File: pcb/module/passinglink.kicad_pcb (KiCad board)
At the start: 2 copper layers, 113.5 x 35 mm, 47 parts, among them J1 Conn_01x05_Female, J10 Conn_02x04_Odd_Even, J11 Conn_01x01, J12 Conn_01x04, J2 Conn_01x04, J3 Conn_02x05_Odd_Even, J4 Conn_01x05, J5 Conn_01x05, J6 Conn_02x08_Odd_Even, J7 Conn_02x08_Odd_Even, J8 Conn_01x03, J9 Conn_01x03, U1 STM32F103RETx, U2 MIC5219-3.3YM5, X1 PCB-USB-C, Y1 Crystal_GND2_Small

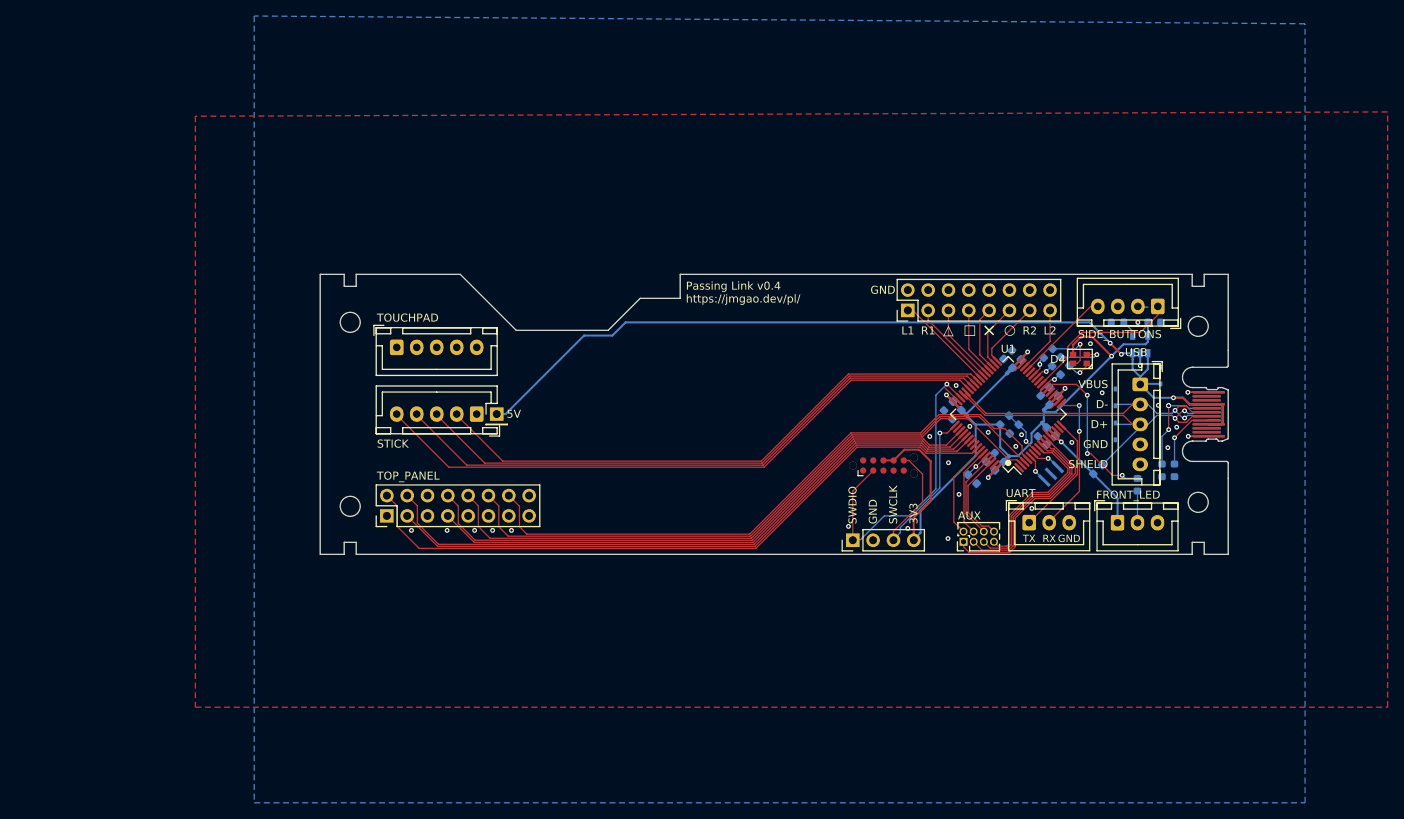
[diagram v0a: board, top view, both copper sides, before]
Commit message: PCB v0.5.
Layout a new PCB that connects to an external breakout board via an M.2
connector.
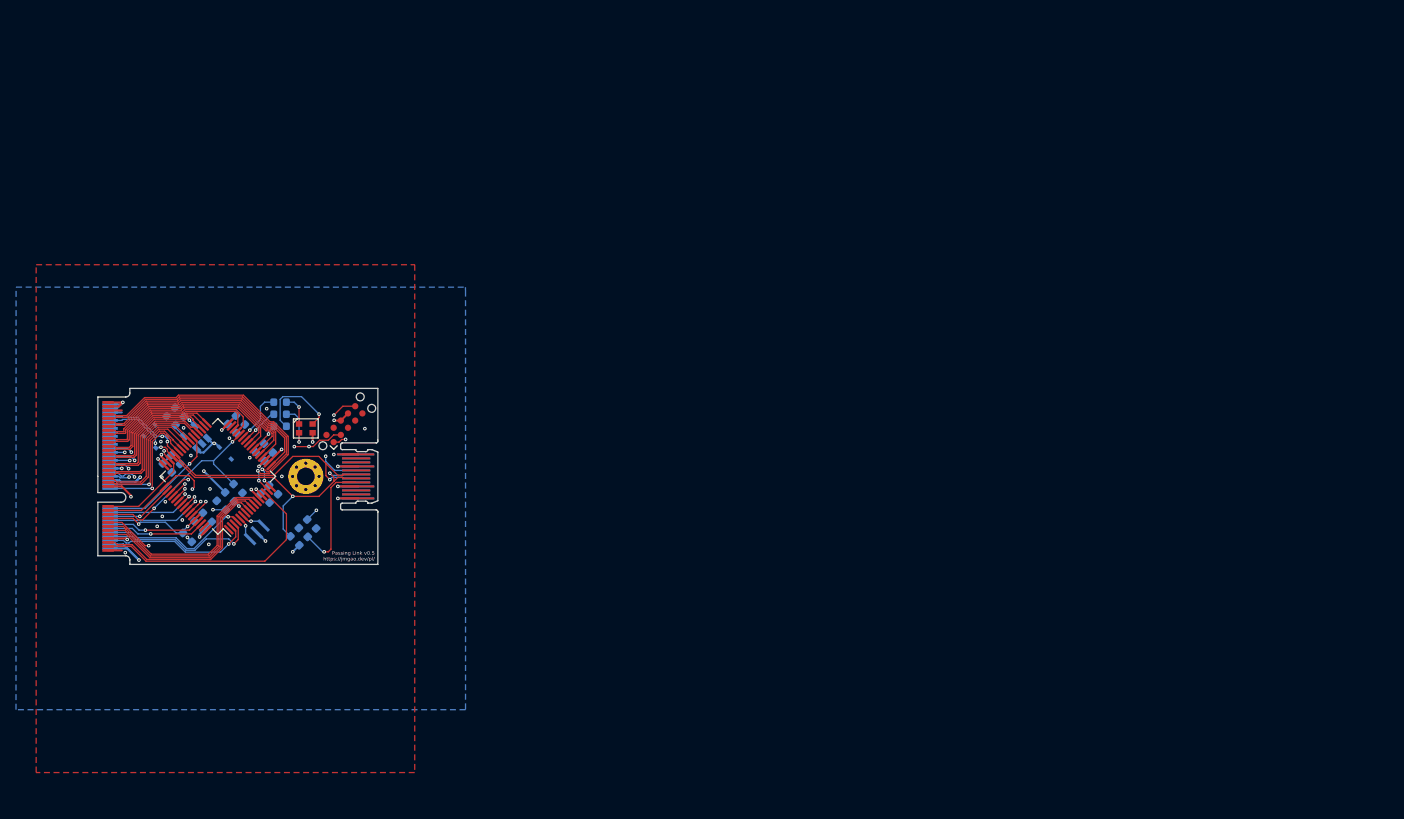
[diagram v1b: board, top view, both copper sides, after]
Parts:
- removed J1: Conn_01x05_Female, Connector_JST:JST_XH_B5B-XH-A_1x05_P2.50mm_Vertical
- removed J10: Conn_02x04_Odd_Even, Connector_PinHeader_1.27mm:PinHeader_2x04_P1.27mm_Vertical
- removed J11: Conn_01x01, Connector_PinHeader_2.54mm:PinHeader_1x01_P2.54mm_Vertical
- removed J12: Conn_01x04, Connector_JST:JST_XH_B4B-XH-A_1x04_P2.50mm_Vertical
- removed J4, J5: Conn_01x05, Connector_JST:JST_XH_B5B-XH-A_1x05_P2.50mm_Vertical
- removed J6, J7: Conn_02x08_Odd_Even, Connector_PinHeader_2.54mm:PinHeader_2x08_P2.54mm_Vertical
- removed J8, J9: Conn_01x03, Connector_JST:JST_XH_B3B-XH-A_1x03_P2.50mm_Vertical
- removed NT1, NT2, NT3, NT4, NT5: Net-Tie_2, NetTie:NetTie-2_SMD_Pad0.5mm
- removed the R4 at (219.6, 99.2)
- removed the R9 at (215.0, 101.0)
- added H1: MountingHole_2.2mm_M2_Pad_Via, MountingHole:MountingHole_2.2mm_M2_Pad_Via, F.Cu at (111.0, 100.0)
- added R1: 10K, Resistor_SMD:R_0603_1608Metric, B.Cu at (102.5, 101.5)
- added R5: 5.1K, Resistor_SMD:R_0603_1608Metric, B.Cu at (110.7, 107.0)
- J2: value Conn_01x04 -> PassingLink; footprint Connector_PinHeader_2.54mm:PinHeader_1x04_P2.54mm_Vertical -> NGFF:NGFF_E
- moved C1 122.4 mm to (95.2, 92.0), turned to 135 degrees
- moved D3 120.7 mm to (91.5, 95.7), turned to 135 degrees
- moved D2 119.4 mm to (92.9, 94.3), turned to 135 degrees
- moved C13 118.9 mm to (94.2, 93.0), turned to 135 degrees
- moved U2 118.6 mm to (97.2, 95.1), turned to 135 degrees
- moved D1 117.3 mm to (100.9, 97.1), turned to -45 degrees
- moved X1 106.6 mm to (120.0, 100.0)
- moved R4 106.5 mm to (111.7, 106.0), turned to -45 degrees
- moved R6 100.8 mm to (109.6, 108.0), turned to -45 degrees
- moved C12 99.6 mm to (100.4, 103.6), turned to 135 degrees
- moved Y1 99.5 mm to (104.9, 107.0)
- moved C7 99.5 mm to (105.3, 97.5)
- moved C5 99.2 mm to (98.7, 105.1)
- moved C10 99.2 mm to (97.6, 106.2)
- moved U1 99.1 mm to (100.0, 100.0)
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- renumbered R1 to R2, R2 to R3, R3 to R4, R5 to R6, R6 to R7, R7 to R8, R8 to R9
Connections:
- C1 pad 1: +3V3 -> VCC1
- C10 pad 1: VCC4 -> VCC1
- C11 pad 1: VDDA -> VCC1
- C3 pad 1: VCC2 -> VCC1
- C4 pad 1: VCC3 -> VCC1
- C5 pad 1: VCC4 -> VCC1
- C6 pad 1: VDDA -> VCC1
- C8 pad 1: VCC2 -> VCC1
- C9 pad 1: VCC3 -> VCC1
- D4 pad 3: +3V3 -> VCC1
- J2 pad 1: SWDIO -> GND
- J2 pad 2: GND -> VCC1
- J2 pad 3: SWCLK -> /PA0_ADC
- J2 pad 4: +3V3 -> VCC1
- J3 pad : GND -> (no net)
- J3 pad 1: Net-(J3-Pad1) -> /NRST
- J3 pad 2: SWDIO -> /PA13_SWDIO
- J3 pad 6: SWCLK -> /PA14_SWCLK
- J3 pad 7: +3V3 -> VCC1
- J3 pad 8: +3V3 -> VCC1
- R2 pad 2: +3V3 -> VCC1
- R6 pad 2: VDDA -> VCC1
- R7 pad 1: /PA7_LED_R_K -> /PB1_LED_R_K
- R9 pad 1: /PB1_LED_B_K -> /PA7_LED_B_K
- U1 pad 10: /PC2 -> /PC2_ADC
- U1 pad 11: /PC3 -> /PC3_ADC
- U1 pad 13: VDDA -> VCC1
- U1 pad 14: /PA0 -> /PA0_ADC
- U1 pad 15: /PA1 -> /PA1_ADC
- U1 pad 16: /PA2_UART_TX -> /PA2_ADC
- U1 pad 17: /PA3_UART_RX -> /PA3_ADC
- U1 pad 2: /PC13_MODE_LS -> /PC13
- U1 pad 20: /PA4 -> /PA4_DAC
- U1 pad 21: /PA5 -> /PA5_DAC
- U1 pad 22: /PA6_FRONT_LED_K -> /PA6_PWM
- U1 pad 23: /PA7_LED_R_K -> /PA7_LED_B_K
- U1 pad 24: /PC4_START -> /PC4_ADC
- U1 pad 25: /PC5 -> /PC5_ADC
- U1 pad 27: /PB1_LED_B_K -> /PB1_LED_R_K
- U1 pad 28: /PB2 -> /BOOT1
- U1 pad 29: /PB10_SELECT -> /PB10_I2C2_SCL
- U1 pad 3: /PC14_MODE_LOCK -> /PC14
- U1 pad 30: /PB11_BUTTON_L2 -> /PB11_I2C2_SDA
- U1 pad 32: VCC2 -> VCC1
- U1 pad 33: /PB12_BUTTON_R2 -> /PB12_SPI1_NSS
- U1 pad 34: /PB13_BUTTON_CIRCLE -> /PB13_SPI1_SCK
- U1 pad 35: /PB14_BUTTON_CROSS -> /PB14_SPI1_MISO
- U1 pad 36: /PB15_BUTTON_SQUARE -> /PB15_SPI1_MOSI
- U1 pad 37: /PC6_BUTTON_TRIANGLE -> /PC6
- U1 pad 38: /PC7_BUTTON_R1 -> /PC7_I2S3_MCK
- U1 pad 39: /PC8_BUTTON_L1 -> /PC8
- U1 pad 4: /PC15_BUTTON_PS4 -> /PC15
- U1 pad 40: /PC9_STICK_RIGHT -> /PC9
- U1 pad 41: /PA8_STICK_LEFT -> /PA8
- U1 pad 42: /PA9_STICK_UP -> /PA9_UART_TX
- U1 pad 43: /PA10_STICK_DOWN -> /PA10_UART_RX
- U1 pad 46: SWDIO -> /PA13_SWDIO
- U1 pad 48: VCC3 -> VCC1
- U1 pad 49: SWCLK -> /PA14_SWCLK
- U1 pad 50: /PA15_JTDI -> /PA15_I2S3_WS
- U1 pad 51: /PC10_MODE_RS -> /PC10
- U1 pad 52: /PC11_MODE_PS3 -> /PC11
- U1 pad 53: /PC12_BUTTON_L3 -> /PC12
- U1 pad 54: /PD2_BUTTON_R3 -> /PD2
- U1 pad 55: /PB3_JTDO -> /PB3_I2S3_CK
- U1 pad 57: /PB5_BUTTON_TOUCHPAD -> /PB5_I2S3_SD
- U1 pad 58: /PB6 -> /PB6_I2C1_SCL
- U1 pad 59: /PB7 -> /PB7_I2C1_SDA
- U1 pad 61: /PB8 -> /PB8_PWM
- U1 pad 62: /PB9 -> /PB9_PWM
- U1 pad 64: VCC4 -> VCC1
- U1 pad 8: /PC0 -> /PC0_ADC
- U1 pad 9: /PC1 -> /PC1_ADC
- U2 pad 5: +3V3 -> VCC1
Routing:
- net +3V3: track 86.6 -> 0.00 mm, vias 1 -> 0
- net /PB5_BUTTON_TOUCHPAD: track 83.9 -> 0.00 mm
- net /PC13_MODE_LS: track 81.5 -> 0.00 mm
- net /PC12_BUTTON_L3: track 79.9 -> 0.00 mm
- net /PA10_STICK_DOWN: track 79.3 -> 0.00 mm
- net /PC14_MODE_LOCK: track 79.2 -> 0.00 mm
- net /PD2_BUTTON_R3: track 78.0 -> 0.00 mm
- net /PC15_BUTTON_PS4: track 77.4 -> 0.00 mm
- net /PA9_STICK_UP: track 77.1 -> 0.00 mm
- net /PA8_STICK_LEFT: track 75.5 -> 0.00 mm
- net /PC10_MODE_RS: track 74.0 -> 0.00 mm
- net /PC9_STICK_RIGHT: track 72.5 -> 0.00 mm
- net /PC11_MODE_PS3: track 72.1 -> 0.00 mm
- net USB_VBUS: track 122.1 -> 73.7 mm, vias 3 -> 4
- net /PA14_SWCLK: track 0.00 -> 39.0 mm, vias 0 -> 2
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- added copper zone on GND, net GND
- added copper zone on PWR, net VCC1
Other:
- board size 113.5 x 35 mm -> 31 x 22 mm
- copper layers 2 -> 4
- net class Default: clearance 0.127 -> 0.0889; via_dia 0.6 -> 0.45; via_drill 0.3 -> 0.2
- net class Power: clearance 0.127 -> 0.0889; via_dia 0.6 -> 0.45; via_drill 0.3 -> 0.2
- net class USB: clearance 0.127 -> 0.0889; via_dia 0.6 -> 0.45; via_drill 0.3 -> 0.2
- rule trace_clearance: 0.127 -> 0.0889
- rule trace_min: 0.127 -> 0.0889
- rule via_min_drill: 0.3 -> 0.2
- rule via_min_size: 0.6 -> 0.45
- board text added: "Passing Link v0.5 https://jmgao.dev/pl/"
- board text removed: "C1-5: 10uF C6: 1uF C7-12: 100nF C13: 470pF"
- board text removed: "D1: 12V D2-3: 5V"
- board text removed: "Passing Link v0.4 https://jmgao.dev/pl/"
- board text removed: "R1-2: 10kΩ R3-4: 5.1kΩ R5: 1.5kΩ R6: 65Ω R7-8: 15Ω"
